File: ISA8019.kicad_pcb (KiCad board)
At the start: 2 copper layers, 157.4 x 74.2 mm, 56 parts, among them J1 Bus_ISA_16bit, J2 8P8C_Shielded, J4 Jumper mode, J5 PNP force, J6 BROM size and base address, J7 I/O base address, J8 Medium type, J9 IRQ select, T1 13F-39MNL, U1 RTL8019AS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

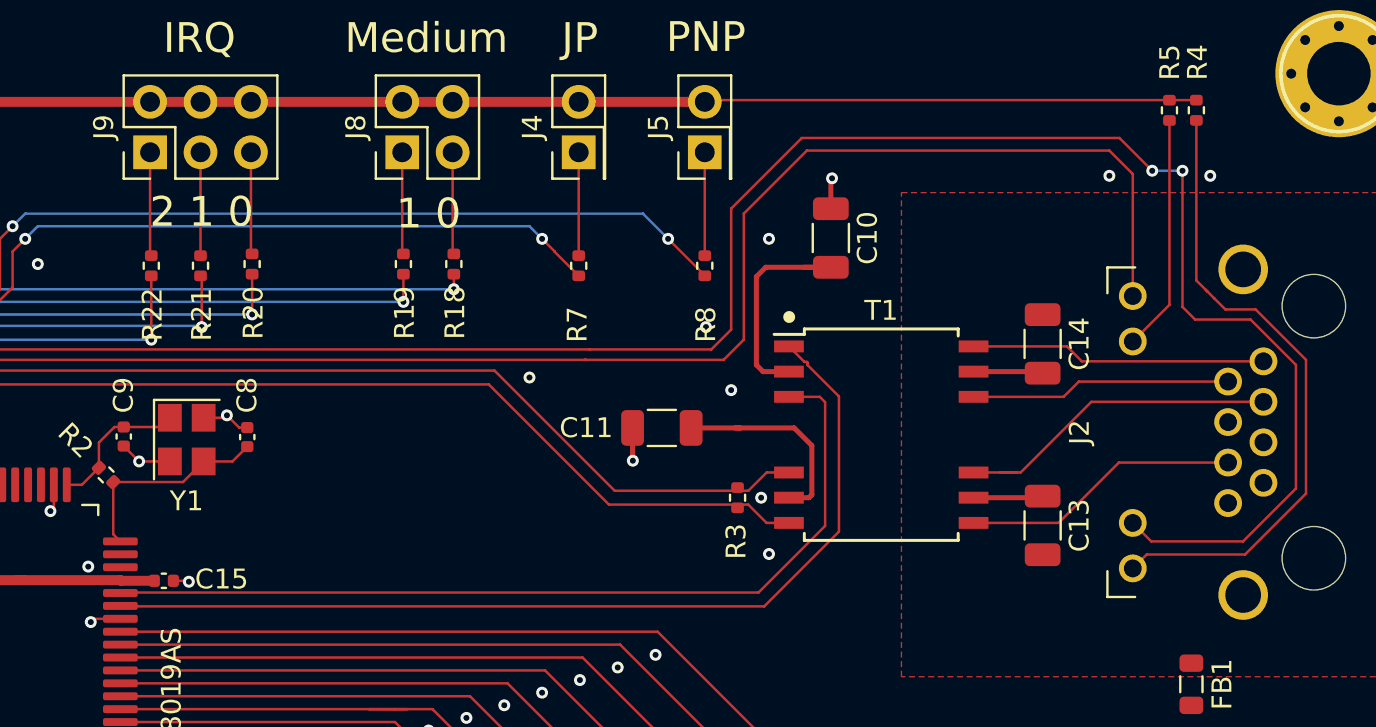
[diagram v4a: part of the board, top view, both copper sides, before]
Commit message: Small trace cleanup and new gerbers
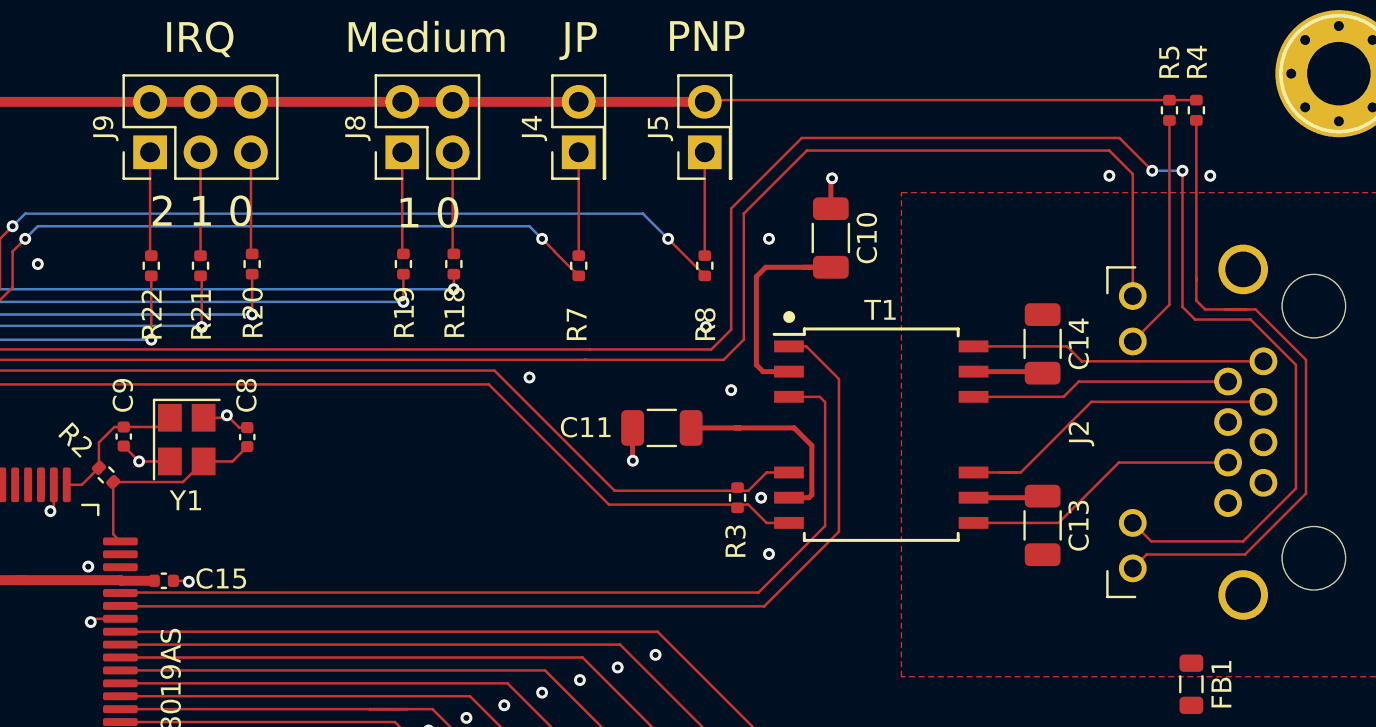
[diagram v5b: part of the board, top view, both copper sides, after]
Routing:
- net Net-(J2-Pad12): track 32.5 -> 34.0 mm
